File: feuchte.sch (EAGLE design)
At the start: 24 parts, among them CON1 CON_PCB_7.5MM_3-POLE, CON2 CON_PCB_7.5MM_3-POLE, IC1 IC_ULN2003AD, IC2 ESD_USB_IP4234CZ6, K1 RELAY_G5LA, K2 RELAY_G5LA, Q1 16MHz, U1 MCU_ATMEGA32U2-AU

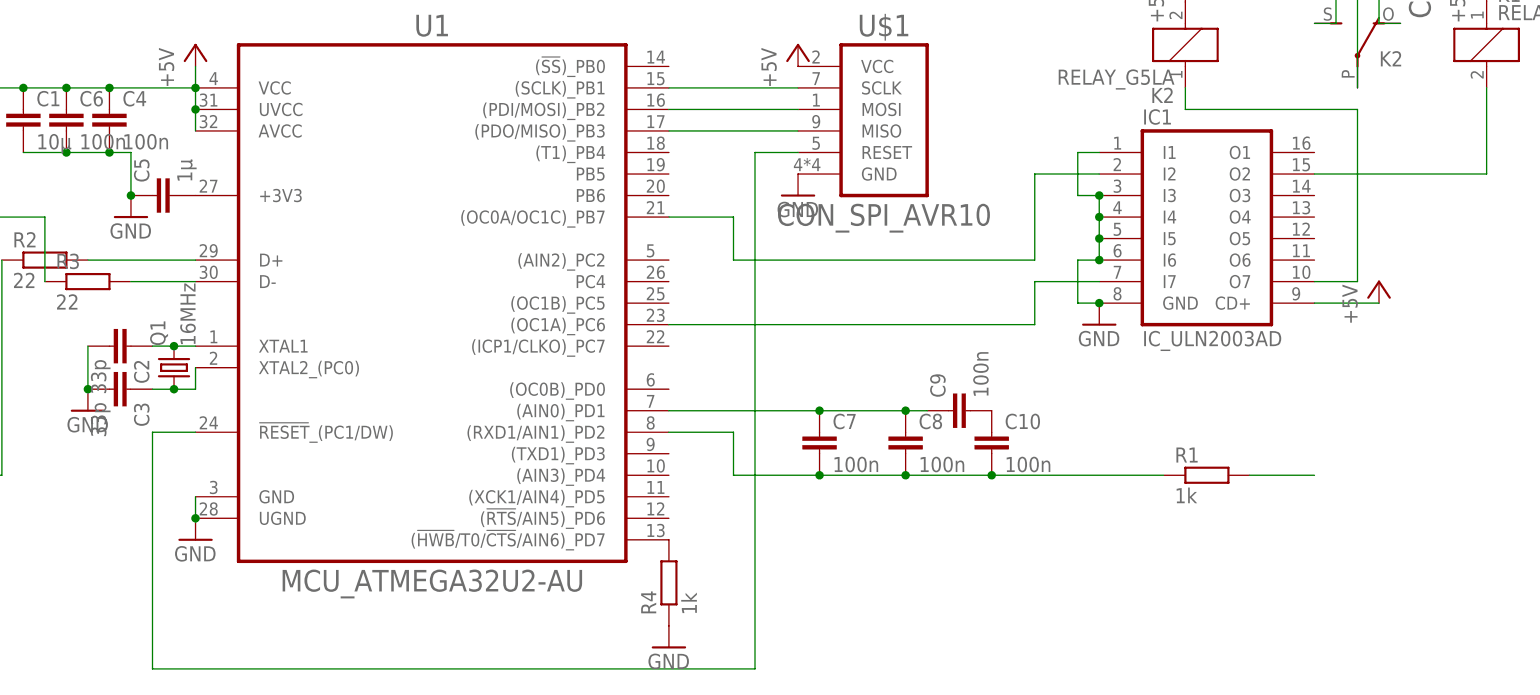
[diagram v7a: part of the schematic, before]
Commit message: 2 Kanäle + SHS-A5 im Schaltplan eingefügt
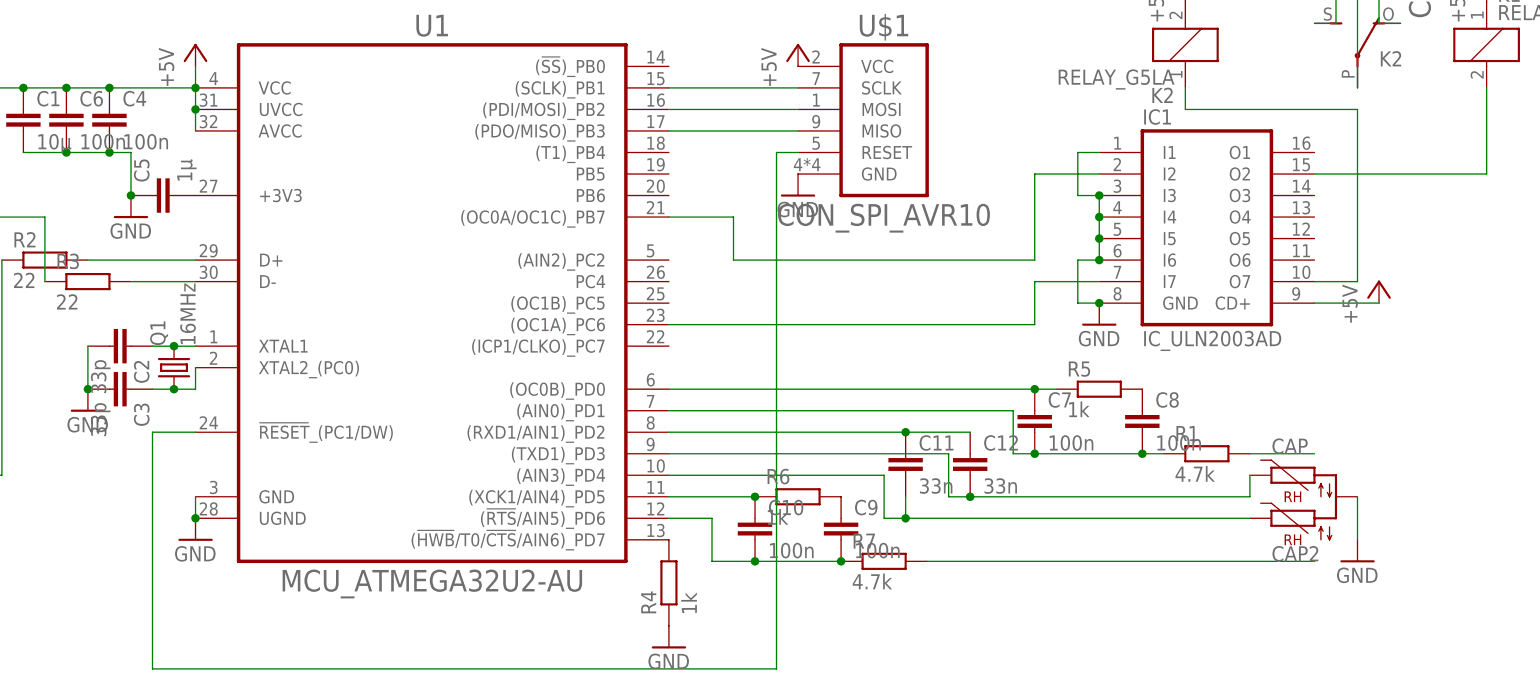
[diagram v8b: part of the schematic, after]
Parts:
- added C11, C12: 33n, Bauelemente:C
- added R5, R6: 1k, Bauelemente:R
- added R7: 4.7k, Bauelemente:R
- added U$2: SENS_SHS-A5, Bauelemente:SENS_SHS-A5
- R1: value 1k -> 4.7k
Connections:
- new net CAP2: R7.2
- new net N$22: C11.1, C12.1, U1.(RXD1/AIN1)_PD2
- new net N$23: C12.2, U$2.3, U1.(TXD1)_PD3
- new net N$24: U1.(OC0B)_PD0
- new net N$25: C11.2, U$2.2, U1.(AIN3)_PD4
- new net N$26: C9.1, R6.2
- new net N$27: C10.1, R6.1, U1.(XCK1/AIN4)_PD5
- new net N$28: C10.2, C9.2, R7.1, U1.(!RTS!/AIN5)_PD6
- net GND: now also U$2.1
- net N$10: now also C8.1, R5.2; no longer C10.1, C9.2
- net N$8: now also R5.1; no longer C8.1, C9.1, U1.(AIN0)_PD1
- net N$9: now also U1.(AIN0)_PD1; no longer C10.2, U1.(RXD1/AIN1)_PD2
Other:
- moved on the sheet: C10, C7, C8, C9, R1
